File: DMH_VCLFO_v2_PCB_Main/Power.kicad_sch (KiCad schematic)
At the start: 11 parts, among them J0 Conn_01x01, J100 IDC_02x05, J11 Conn_01x08

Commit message: Improved inter-PCB connections
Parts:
- added C23, C24, C3, C4: 100nF, Capacitor_THT:C_Disc_D4.3mm_W1.9mm_P5.00mm, symbol Device:C
- added U1, U2: TL074, symbol Amplifier_Operational:TL074
- renumbered J11 to J300
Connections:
- net +12V: now also C23.1, C3.1, U1.4 (V+), U2.4 (V+)
- net -12V: now also C24.2, C4.2, U1.11 (V-), U2.11 (V-)
- net GND: now also C23.2, C24.1, C3.2, C4.1

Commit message: Notes from breadboarding
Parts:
- U1, U2: footprint (none) -> Package_DIP:DIP-14_W7.62mm_Socket
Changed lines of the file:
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@@
 			)
 		)
-		(property "Footprint" ""
+		(property "Footprint" "Package_DIP:DIP-14_W7.62mm_Socket"
 			(at 64.77 118.11 0)
 			(effects
@@
 			)
 		)
-		(property "Footprint" ""
+		(property "Footprint" "Package_DIP:DIP-14_W7.62mm_Socket"
 			(at 39.37 118.11 0)
 			(effects

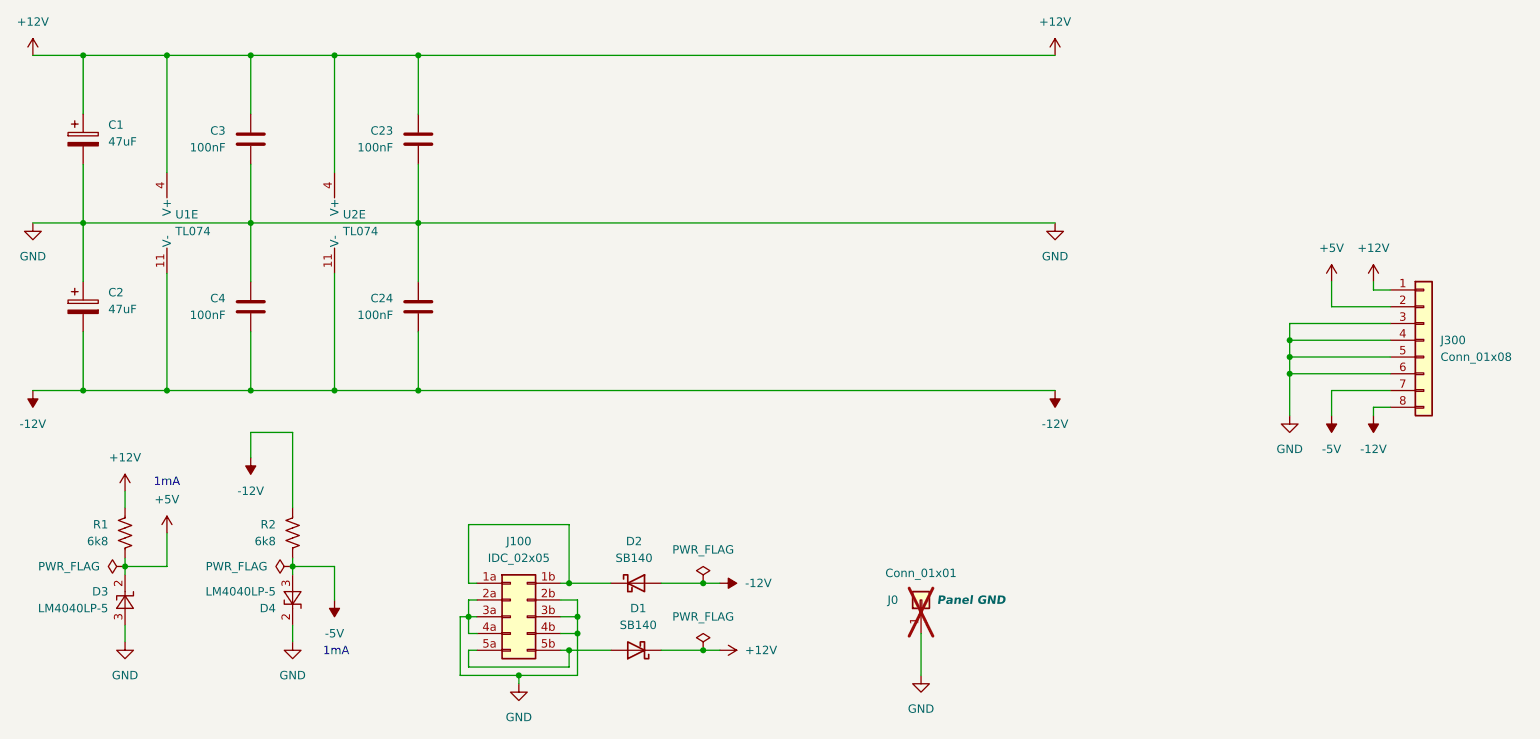
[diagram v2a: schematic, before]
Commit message: Redesigned schematic for V/Oct
And also Bus CV and Fine tune
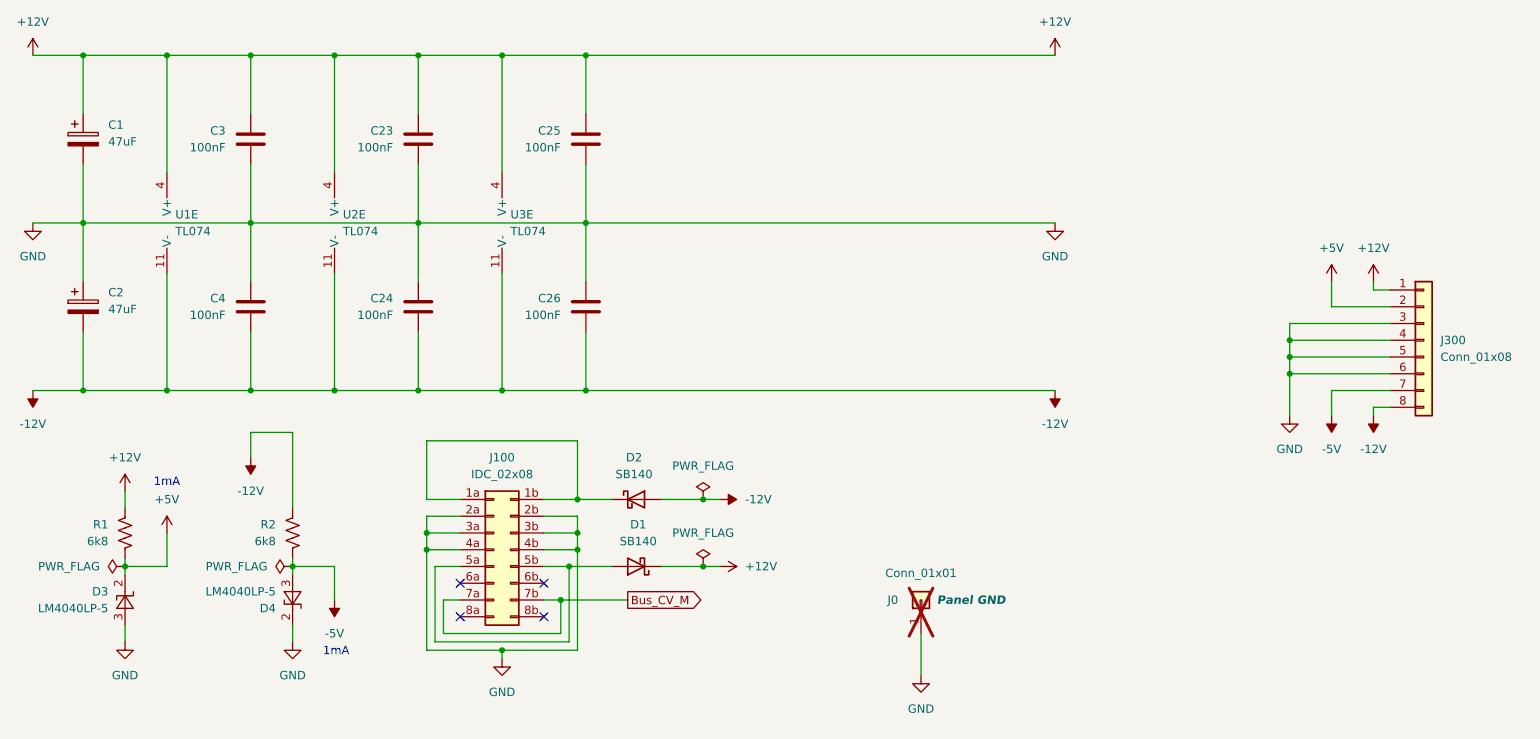
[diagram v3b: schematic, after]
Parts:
- removed J100: IDC_02x05, SynthStuff:IDC-Header_2x05_P2.54mm_Vertical_Eurorack, symbol SynthStuff:Eurorack_Power_Connector_10Pin
- added C25, C26: 100nF, Capacitor_THT:C_Disc_D4.3mm_W1.9mm_P5.00mm, symbol Device:C
- added J100: IDC_02x08, SynthStuff:IDC-Header_2x08_P2.54mm_Vertical_Eurorack, symbol SynthStuff:Eurorack_Power_Connector_16Pin
- added U3: TL074, Package_DIP:DIP-14_W7.62mm_Socket, symbol Amplifier_Operational:TL074
- U1: footprint Package_DIP:DIP-14_W7.62mm_Socket -> (none)
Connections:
- net +12V: now also C25.1, U3.4 (V+)
- net -12V: now also C26.2, U3.11 (V-)
- net GND: now also C25.2, C26.1, J100.2a (Pin_2a), J100.2b (Pin_2b), J100.3a (Pin_3a), J100.3b (Pin_3b), J100.4a (Pin_4a), J100.4b (Pin_4b)
- net at D2.1 (K): now also J100.1a (Pin_1a), J100.1b (Pin_1b)
- net at D1.2 (A): now also J100.5a (Pin_5a), J100.5b (Pin_5b)
- new net Bus_CV_M: J100.7a (Pin_7a), J100.7b (Pin_7b)
- no-connect marks 0 -> 4
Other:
- moved on the sheet: D1, D2
